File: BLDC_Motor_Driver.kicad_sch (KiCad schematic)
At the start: 9 parts, among them IC8 TPS7A4901DGNT, J2 031-5431-10RFX, J3 031-5431-10RFX

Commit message: Initial layout
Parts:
- added H1, H2, H3, H4: MountingHole_Pad, MountingHole:MountingHole_3.2mm_M3_DIN965_Pad, symbol Mechanical:MountingHole_Pad
- added H5, H6, H7, H8: MountingHole, MountingHole:MountingHole_4.3mm_M4, symbol Mechanical:MountingHole
- added J4, J5: 031-5431-10RFX, BLDC-Motor-Driver:031543110RFX, symbol BLDC-Motor-Driver_v2:031-5431-10RFX
- added J6: Conn_01x06_Pin, Connector_PinHeader_2.54mm:PinHeader_1x06_P2.54mm_Vertical, symbol Connector:Conn_01x06_Pin
- C21, C22, C23, C24: footprint (none) -> Capacitor_SMD:C_0603_1608Metric
- R17, R18: footprint (none) -> Resistor_SMD:R_0603_1608Metric
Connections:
- net GND: now also J2.1, H4.1, J4.1, J5.1, J6.2 (Pin_2), J6.4 (Pin_4), J6.6 (Pin_6); no longer J2.2
- net VBUS: now also J2.2; no longer J2.1
- new net Microcontroller/BENCHMARK_IO_1: J6.1 (Pin_1)
- new net Microcontroller/BENCHMARK_IO_2: J6.3 (Pin_3)
- new net Microcontroller/BENCHMARK_IO_3: J6.5 (Pin_5)
- new net Microcontroller/SERCOM3_PAD2: J4.2
- new net Microcontroller/SERCOM4_PAD2: J5.2
- no-connect marks 5 -> 12
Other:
- sheet Current Sensing Differencel Amplifier renamed Current Sensing Difference Amplifier
- sheet Current Sensing Difference Amplifier ports: added CSA_PH_A_IN+, CSA_PH_A_IN-, CSA_PH_A_VOUT, CSA_PH_B_IN+, CSA_PH_B_IN-, CSA_PH_B_VOUT, CSA_PH_C_IN+, CSA_PH_C_IN-, CSA_PH_C_VOUT; removed none
- sheet Microcontroller ports: added ADC_AIN4, ADC_AIN5, ADC_AIN6, BENCHMARK_IO_1, BENCHMARK_IO_2, BENCHMARK_IO_3, SERCOM3_PAD1, SERCOM3_PAD2, SERCOM4_PAD1, SERCOM4_PAD2, SERCOM5_PAD0, SERCOM5_PAD1, SERCOM5_PAD2, SERCOM5_PAD3, TCC0_WO0, TCC0_WO1, TCC0_WO2, TCC0_WO4, TCC0_WO5, TCC0_WO6; removed none
- sheet Position Sensor - Magnetic Encoder ports: added ENCODER_CSn, ENCODER_MISO, ENCODER_MOSI, ENCODER_SCLK; removed none
- sheet Power Stage - Inverter & Gate Drivers ports: added DIFF_AMP_PH_A_IN+, DIFF_AMP_PH_A_IN-, DIFF_AMP_PH_B_IN+, DIFF_AMP_PH_B_IN-, DIFF_AMP_PH_C_IN+, DIFF_AMP_PH_C_IN-, HALF_BRIDGE_PH_A_HI, HALF_BRIDGE_PH_A_LO, HALF_BRIDGE_PH_B_HI, HALF_BRIDGE_PH_B_LO, HALF_BRIDGE_PH_C_HI, HALF_BRIDGE_PH_C_LO, OUT_PHASE_A, OUT_PHASE_B, OUT_PHASE_C; removed none
- moved on the sheet: C21, C22, C23, C24, IC8, J2, J3, R17, R18

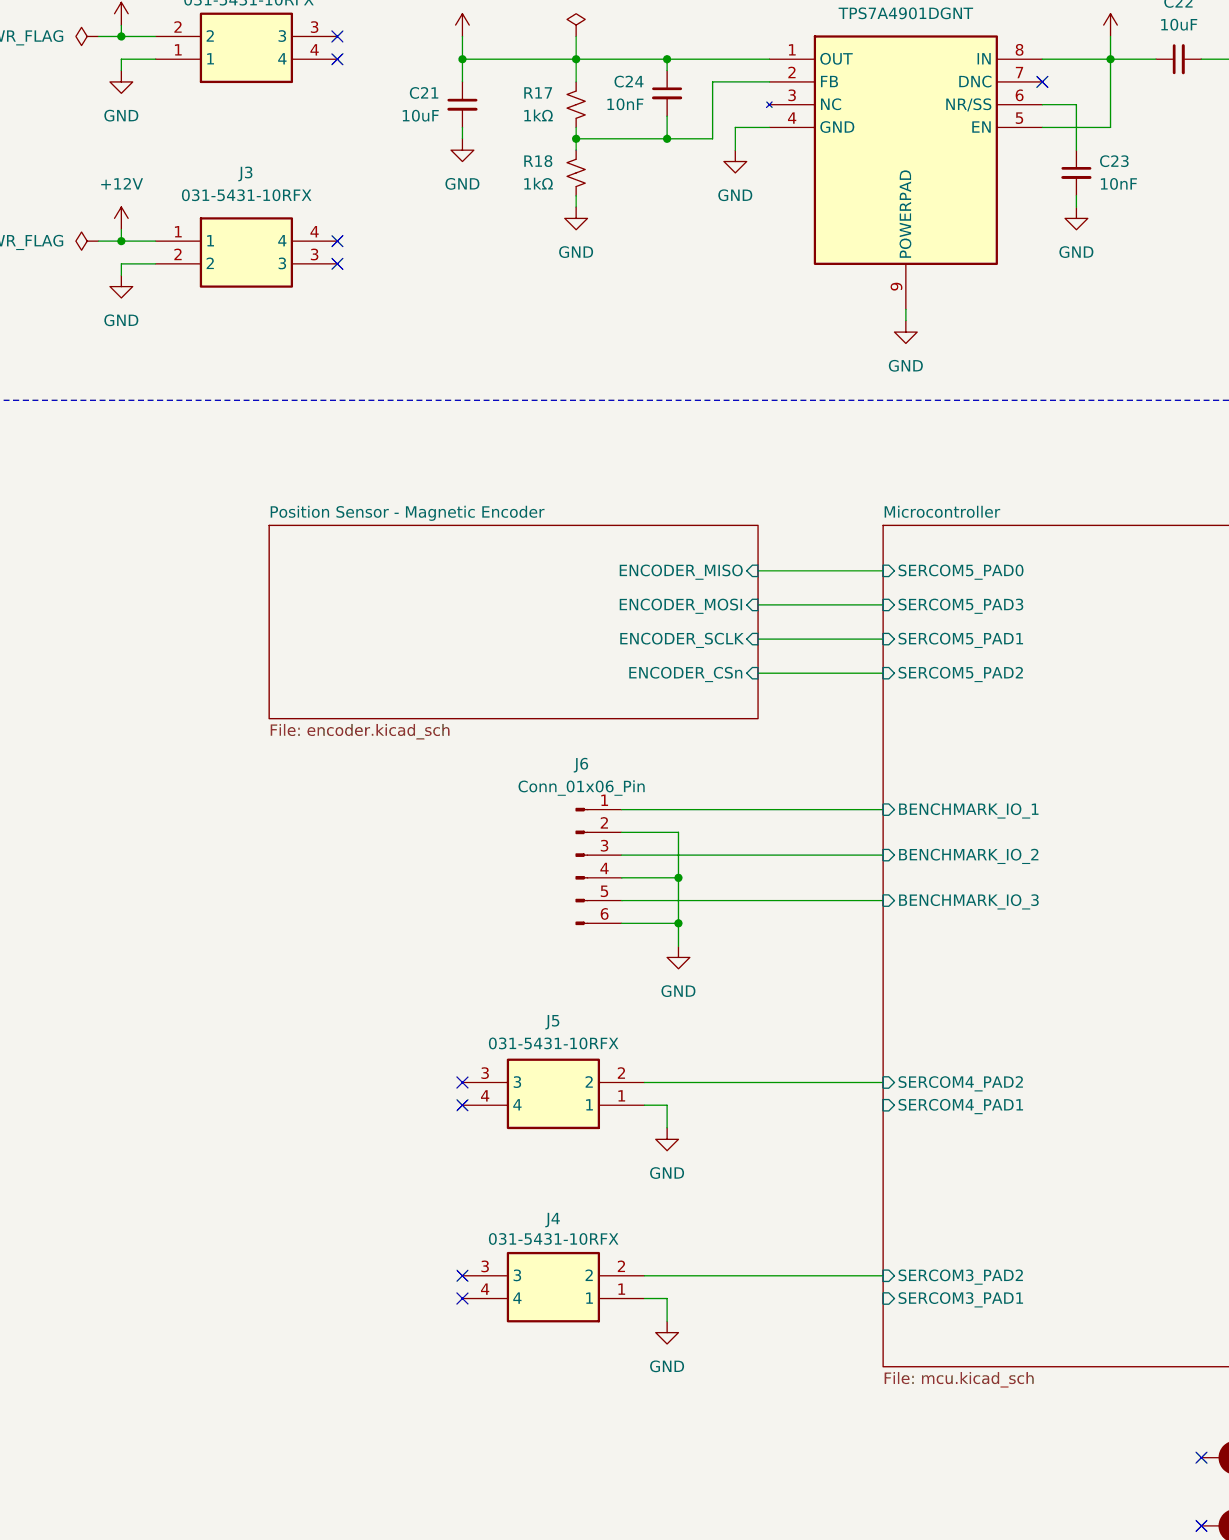
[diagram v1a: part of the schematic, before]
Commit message: Almost all routing done
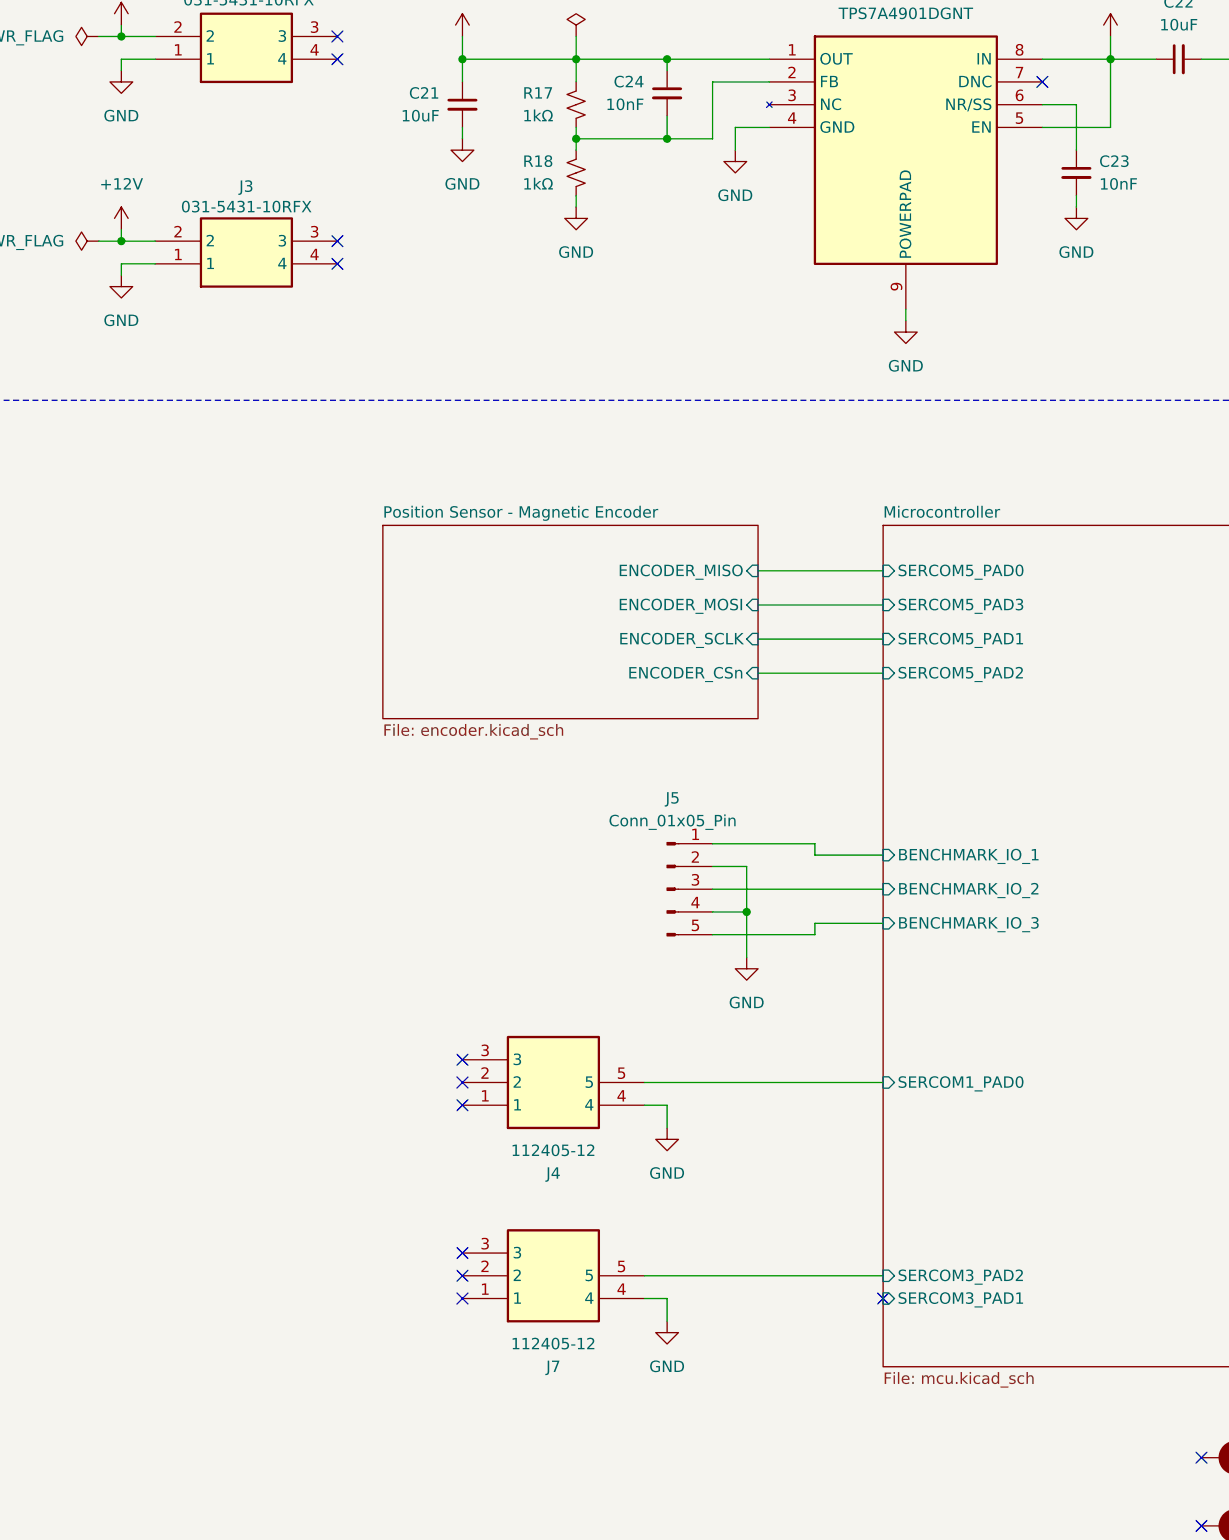
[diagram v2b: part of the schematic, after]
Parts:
- removed J4, J5: 031-5431-10RFX, BLDC-Motor-Driver:031543110RFX, symbol BLDC-Motor-Driver_v2:031-5431-10RFX
- removed J6: Conn_01x06_Pin, Connector_PinHeader_2.54mm:PinHeader_1x06_P2.54mm_Vertical, symbol Connector:Conn_01x06_Pin
- added J4, J7: 112405-12, BLDC-Motor-Driver:11240512, symbol BLDC-Motor-Driver_v2:112405-12
- added J5: Conn_01x05_Pin, Connector_PinHeader_1.27mm:PinHeader_1x05_P1.27mm_Vertical, symbol Connector:Conn_01x05_Pin
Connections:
- net +12V: now also J3.2; no longer J3.1
- net GND: now also J3.1, J4.4, J5.2 (Pin_2), J5.4 (Pin_4), J7.4; no longer J3.2
- net Microcontroller/BENCHMARK_IO_1: now also J5.1 (Pin_1)
- net Microcontroller/BENCHMARK_IO_2: now also J5.3 (Pin_3)
- net Microcontroller/BENCHMARK_IO_3: now also J5.5 (Pin_5)
- net Microcontroller/SERCOM3_PAD2: now also J7.5
- new net Microcontroller/SERCOM1_PAD0: J4.5
- no-connect marks 12 -> 15
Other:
- sheet Microcontroller ports: added SERCOM1_PAD0; removed SERCOM4_PAD1, SERCOM4_PAD2

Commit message: More routing
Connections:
- net Microcontroller/SERCOM3_PAD2 renamed Microcontroller/SERCOM4_PAD0
- no-connect marks 15 -> 14
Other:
- sheet Microcontroller ports: added SERCOM4_PAD0; removed SERCOM3_PAD1, SERCOM3_PAD2
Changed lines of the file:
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@@
 	)
 	(no_connect
-		(at 116.84 176.53)
-	)
-	(no_connect
 		(at 152.4 209.55)
 	)
@@
 			)
 		)
-		(pin "SERCOM3_PAD1" input
-			(at 116.84 176.53 180)
-			(effects
-				(font
-					(size 1.27 1.27)
-				)
-				(justify left)
-			)
-		)
-		(pin "SERCOM3_PAD2" input
-			(at 116.84 173.99 180)
-			(effects
-				(font
-					(size 1.27 1.27)
-				)
-				(justify left)
-			)
-		)
 		(pin "SERCOM5_PAD0" input
 			(at 116.84 95.25 180)
@@
 			(effects
 				(font
+					(size 1.27 1.27)
+				)
+				(justify left)
+			)
+		)
+		(pin "SERCOM4_PAD0" input
+			(at 116.84 173.99 180)
+			(effects
+				(font

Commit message: Add capacitors
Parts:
- added C7, C9: 220uF, BLDC-Motor-Driver:CAPAE1030X1050N, symbol Device:C_Polarized
- added J6: Conn_01x04_Socket, BLDC-Motor-Driver:SHDR4W91P0X350_1X4_1400X730X875P, symbol Connector:Conn_01x04_Socket
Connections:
- net +12V: now also C7.1
- net GND: now also C7.2, C9.2, J6.4 (Pin_4)
- net Power Stage - Inverter & Gate Drivers/OUT_PHASE_A: now also J6.1 (Pin_1)
- net Power Stage - Inverter & Gate Drivers/OUT_PHASE_B: now also J6.2 (Pin_2)
- net Power Stage - Inverter & Gate Drivers/OUT_PHASE_C: now also J6.3 (Pin_3)
- net VBUS: now also C9.1
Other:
- moved on the sheet: C21, C22, C23, C24, IC8, J2, J3, R17, R18

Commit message: Add 5V rail available for LDO input
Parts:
- removed H5, H6, H7, H8: MountingHole, MountingHole:MountingHole_4.3mm_M4, symbol Mechanical:MountingHole
- added C15: 47uF, BLDC-Motor-Driver:CAPAE660X770N, symbol Device:C_Polarized
- added H5, H6, H7, H8: MountingHole_Pad, MountingHole:MountingHole_3.2mm_M3_DIN965_Pad, symbol Mechanical:MountingHole_Pad
- added J8: 031-5431-10RFX, BLDC-Motor-Driver:031543110RFX, symbol BLDC-Motor-Driver_v2:031-5431-10RFX
- added J9: Conn_01x03_Pin, Connector_PinHeader_2.54mm:PinHeader_1x03_P2.54mm_Vertical, symbol Connector:Conn_01x03_Pin
- C7: value 220uF -> 100uF; footprint BLDC-Motor-Driver:CAPAE1030X1050N -> BLDC-Motor-Driver:CAPAE830X1050N
- H1, H2, H3, H4: footprint MountingHole:MountingHole_3.2mm_M3_DIN965_Pad -> MountingHole:MountingHole_4.3mm_M4_DIN965_Pad_TopBottom
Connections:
- net +12V: now also J9.3 (Pin_3); no longer C22.1, IC8.5 (EN), IC8.8 (IN)
- net GND: now also C15.2, H8.1, J8.1
- new net +5V: C15.1, J8.2, J9.1 (Pin_1)
- new net LDO_INPUT: C22.1, IC8.5 (EN), IC8.8 (IN), J9.2 (Pin_2)
- no-connect marks 14 -> 19
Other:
- note added: "Select the LDO input voltage by using a jumper socket"
- moved on the sheet: C21, C22, C23, C24, C7, C9, H1, IC8, J2, J3, J4, J5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
